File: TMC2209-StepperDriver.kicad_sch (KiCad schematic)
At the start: 4 parts, among them J4 Conn_01x04

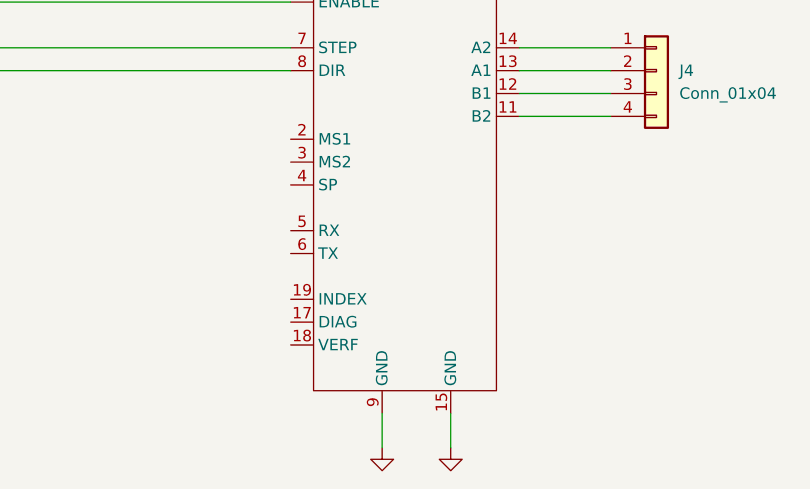
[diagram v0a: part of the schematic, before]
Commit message: Boardconfig update
updated board config
updated outline
moved USB and battery connections
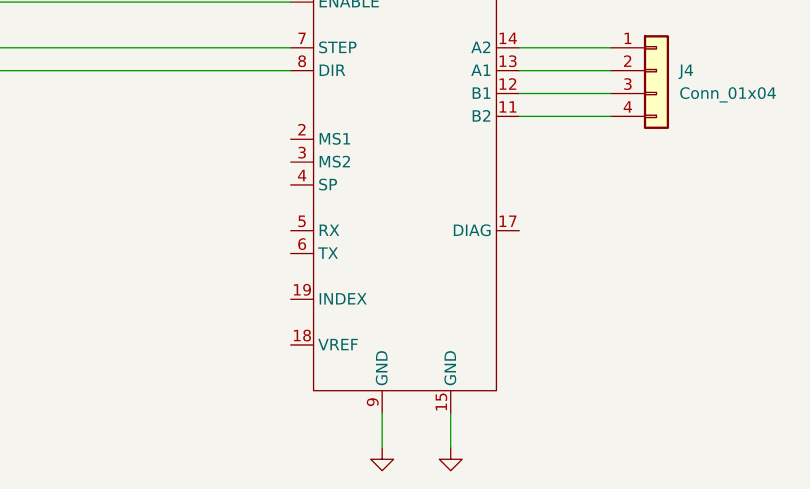
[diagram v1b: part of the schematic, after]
